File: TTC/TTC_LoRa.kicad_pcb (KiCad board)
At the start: 2 copper layers, 70 x 70 mm, 78 parts, among them J1 EPS 3V3, J2 MISSION, J3 SMA edge, J4 SWD TC2030, J5 OBC I2C, J6 OBC UART, J7 EPS 5V, J8 SPARE GPIO, J9 DIPOLE FEED, Q1 AO3401A, U1 TPS7A2033PDBVR, U2 RFM98W-433S2, U3 STM32F446RET6, U4 TMP102, Y1 8MHz, Y2 32.768kHz

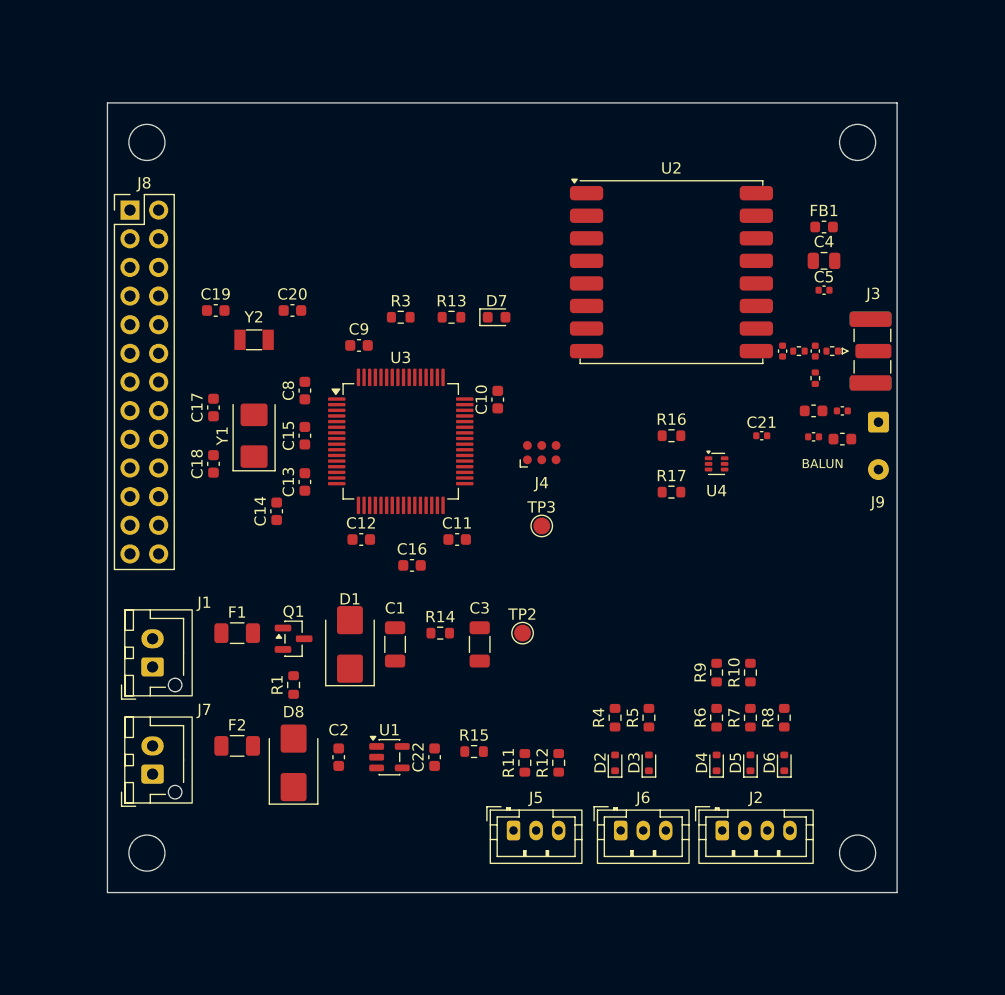
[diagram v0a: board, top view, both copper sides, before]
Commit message: TTC: fully routed LoRa board (checkpoint before review fixes)
Routed 2-layer layout of the TTC board: 1207 tracks, 297 vias, GND
poured on both layers. KiCad DRC: 0 violations, 0 unconnected,
schematic parity clean. README updated from "placed, not routed".

Co-Authored-By: Claude Opus 5.5 <noreply@anthropic.com>
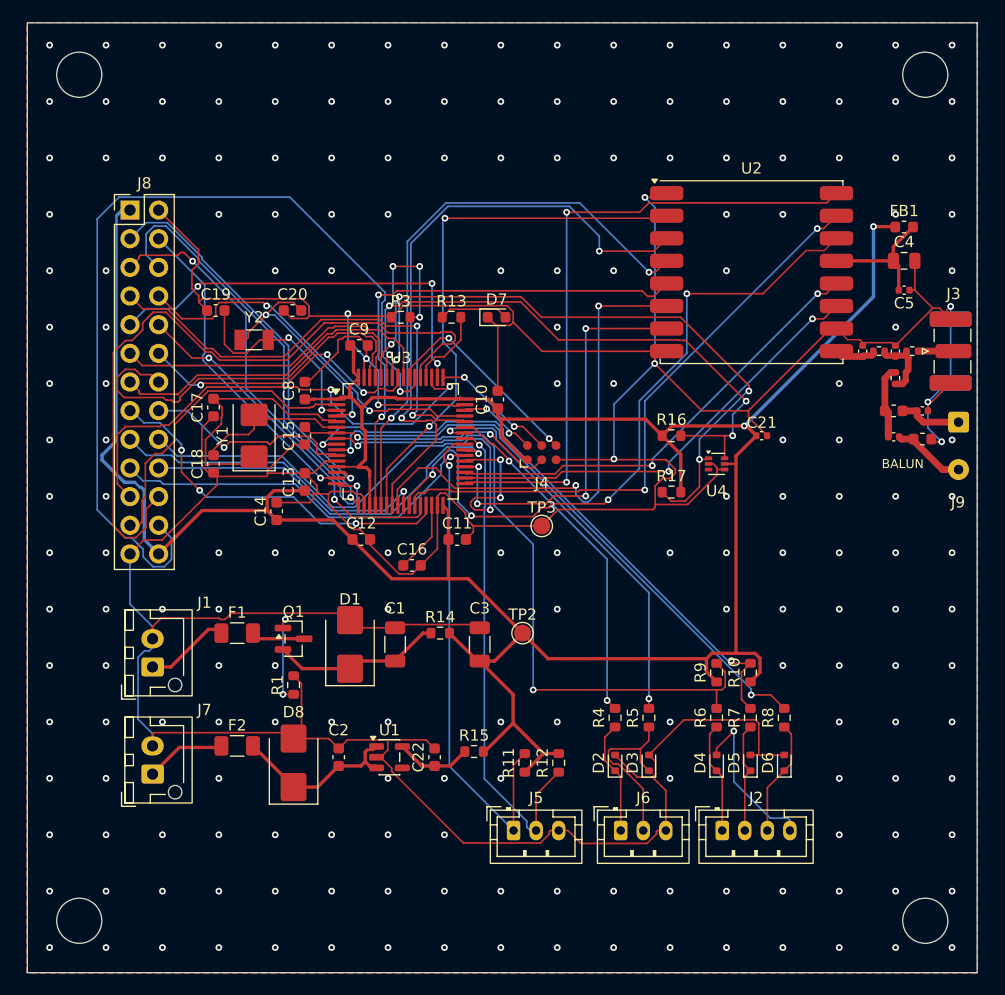
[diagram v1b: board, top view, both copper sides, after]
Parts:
- H1, H2, H3, H4: value M3 -> M4 stack; footprint MountingHole_3.2mm_M3 -> MountingHole_4mm
- moved H1 8.49 mm to (97.5, 97.5)
- moved H2 8.49 mm to (172.5, 97.5)
- moved H3 8.49 mm to (97.5, 172.5)
- moved H4 8.49 mm to (172.5, 172.5)
- moved C23 7.10 mm to (172.2, 127.3)
- moved C24 7.10 mm to (169.7, 129.6)
- moved C4 7.10 mm to (170.6, 114.0)
- moved C5 7.10 mm to (170.6, 116.6)
- moved C6 7.10 mm to (166.9, 122.0)
- moved C7 7.10 mm to (169.8, 122.0)
- moved FB1 7.10 mm to (170.6, 111.0)
- moved J3 7.10 mm to (175.0, 122.0)
- moved J9 7.10 mm to (175.4, 128.3)
- moved L1 7.10 mm to (169.7, 127.3)
- moved L2 7.10 mm to (172.2, 129.8)
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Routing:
- net GND: track 0.00 -> 457.0 mm, vias 0 -> 201
- net +3V3: track 0.00 -> 254.4 mm, vias 0 -> 2
- net /PD2: track 0.00 -> 80.2 mm, vias 0 -> 1
- net /PC12: track 0.00 -> 63.5 mm
- net /RFM_DIO0: track 0.00 -> 62.5 mm, vias 0 -> 4
- net /DEPLOY_SW: track 0.00 -> 59.2 mm, vias 0 -> 2
- net /RFM_DIO2: track 0.00 -> 57.6 mm, vias 0 -> 2
- net /I2C_SCL: track 0.00 -> 57.5 mm, vias 0 -> 4
- net /SPI1_MOSI: track 0.00 -> 54.9 mm, vias 0 -> 2
- net /RBF_IN: track 0.00 -> 54.2 mm, vias 0 -> 2
- net /RFM_DIO1: track 0.00 -> 53.3 mm, vias 0 -> 2
- net /BURN_EN: track 0.00 -> 52.8 mm, vias 0 -> 2
- net /I2C_SDA: track 0.00 -> 52.3 mm, vias 0 -> 4
- net /PC6: track 0.00 -> 51.9 mm, vias 0 -> 3
- net /SPI1_SCK: track 0.00 -> 51.7 mm, vias 0 -> 2
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- added copper zone on B.Cu, net GND
- added copper zone on F.Cu, net GND
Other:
- board size 70 x 70 mm -> 84.2 x 84.2 mm

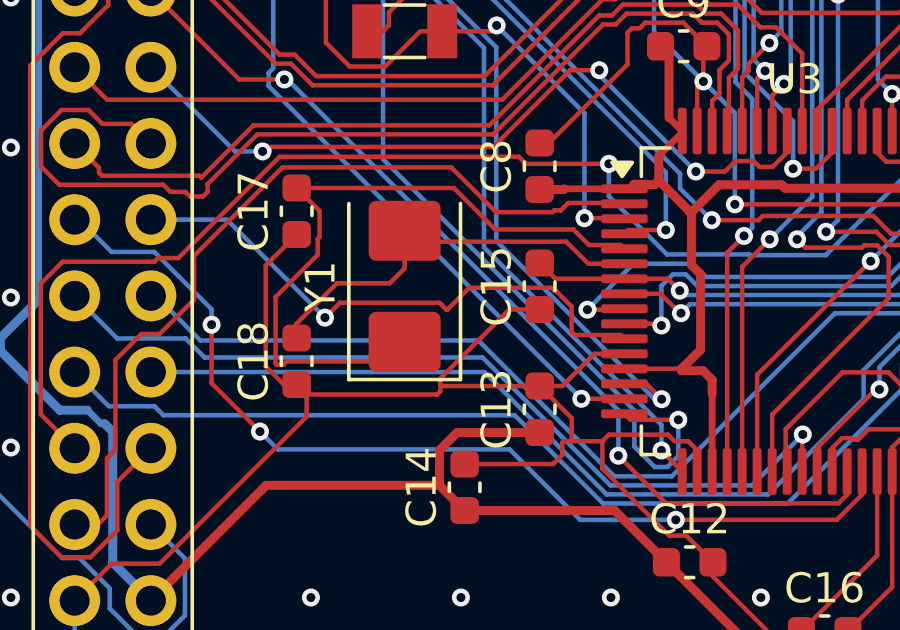
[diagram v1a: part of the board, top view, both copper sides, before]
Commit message: TTC: re-route 8 MHz crystal (Y1 rotated 180 deg)
Y1's pads were mirrored relative to the MCU pins, so PH0/PH1 crossed
and detoured. Rotating Y1 lines them up: PH0 23.2 -> 11.8 mm,
PH1 13.9 -> 16.7 mm (goes round the PC3 track), total 37.1 -> 28.5 mm,
no crossing. DRC: 0 violations, 0 unconnected.

Co-Authored-By: Claude Opus 5.5 <noreply@anthropic.com>
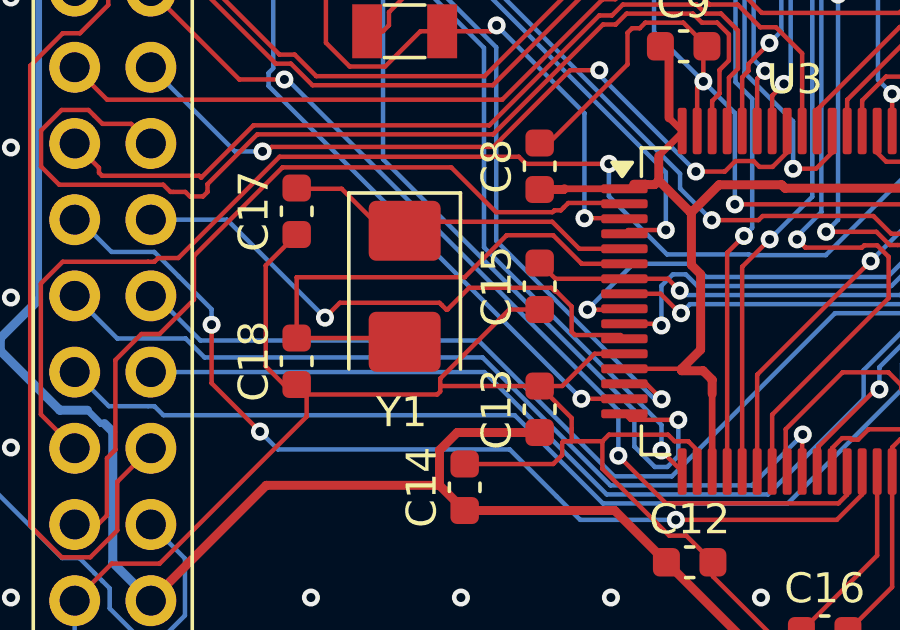
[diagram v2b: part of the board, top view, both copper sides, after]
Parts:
- turned Y1 to -90 degrees
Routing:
- net Net-(U3-PH0): track 23.2 -> 11.8 mm
- net Net-(U3-PH1): track 13.9 -> 16.7 mm
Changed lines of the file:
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@@
 	(footprint "Crystal:Crystal_SMD_5032-2Pin_5.0x3.2mm"
 		(layer "F.Cu")
-		(at 113 129.5 90)
+		(at 113 129.5 -90)
 		(descr "8 MHz HSE crystal (2-pad 5032); load caps from its CL")
 		(property "Reference" "Y1"
-			(at 0 -2.8 90)
+			(at 4.199999 0.1 0)
 			(layer "F.SilkS")
 			(effects
@@
 		)
 		(property "Value" "8MHz"
-			(at 0 2.8 90)
+			(at 0 2.8 270)
 			(layer "F.Fab")
 			(effects
@@
 		)
 		(property "Datasheet" ""
-			(at 0 0 90)
+			(at 0 0 270)
 			(layer "F.Fab")
 			(hide yes)
@@
 		)
 		(property "Description" "8 MHz HSE crystal (2-pad 5032); load caps from its CL"
-			(at 0 0 90)
+			(at 0 0 270)
 			(layer "F.Fab")
 			(hide yes)
@@
 		(duplicate_pad_numbers_are_jumpers no)
 		(fp_line
-			(start 2.76 -1.86)
-			(end -3.11 -1.86)
+			(start -3.11 1.86)
+			(end 2.76 1.86)
 			(stroke
 				(width 0.12)
@@
 		)
 		(fp_line
-			(start -3.11 1.86)
-			(end 2.76 1.86)
+			(start 2.76 -1.86)
+			(end -3.11 -1.86)
 			(stroke
 				(width 0.12)
@@
 		)
 		(fp_text user "${REFERENCE}"
-			(at 0 0 90)
+			(at 0 0 270)
 			(layer "F.Fab")
 			(effects
@@
 		)
 		(pad "1" smd roundrect
-			(at -1.85 0 90)
+			(at -1.85 0 270)
 			(size 2 2.4)
 			(layers "F.Cu" "F.Mask" "F.Paste")
@@
 		)
 		(pad "2" smd roundrect
-			(at 1.85 0 90)
+			(at 1.85 0 270)
 			(size 2 2.4)
 			(layers "F.Cu" "F.Mask" "F.Paste")
@@
 	)
 	(segment
-		(start 109.0579 132.0083)
-		(end 112.3417 132.0083)
-		(width 0.15)
-		(layer "F.Cu")
-		(net "Net-(U3-PH0)")
-	)
-	(segment
-		(start 110.1011 128.4511)
-		(end 108.6974 129.8548)
-		(width 0.15)
-		(layer "F.Cu")
-		(net "Net-(U3-PH0)")
-	)
-	(segment
-		(start 119.2406 128.1255)
-		(end 120.2005 128.1255)
-		(width 0.15)
-		(layer "F.Cu")
-		(net "Net-(U3-PH0)")
-	)
-	(segment
-		(start 109.4 126.225)
-		(end 114.6398 126.225)
-		(width 0.15)
-		(layer "F.Cu")
-		(net "Net-(U3-PH0)")
-	)
-	(segment
-		(start 112.3417 132.0083)
-		(end 113 131.35)
-		(width 0.15)
-		(layer "F.Cu")
-		(net "Net-(U3-PH0)")
-	)
-	(segment
-		(start 110.1633 127.8546)
-		(end 110.1011 127.9168)
-		(width 0.15)
-		(layer "F.Cu")
-		(net "Net-(U3-PH0)")
-	)
-	(segment
-		(start 109.4 126.225)
-		(end 110.1633 126.9883)
-		(width 0.15)
-		(layer "F.Cu")
-		(net "Net-(U3-PH0)")
-	)
-	(segment
-		(start 110.1011 127.9168)
-		(end 110.1011 128.4511)
+		(start 120.325 128.25)
+		(end 118.82 128.25)
 		(width 0.15)
 		(layer "F.Cu")
@@
 	)
 	(segment
-		(start 108.6974 129.8548)
-		(end 108.6974 132.0724)
+		(start 117.92 127.35)
+		(end 112 127.35)
 		(width 0.15)
 		(layer "F.Cu")
@@
 	)
 	(segment
-		(start 118.6233 127.6062)
-		(end 119.1426 128.1255)
+		(start 110.9 126.25)
+		(end 109.4 126.25)
 		(width 0.15)
 		(layer "F.Cu")
@@
 	)
 	(segment
-		(start 108.7395 132.1145)
-		(end 108.9517 132.1145)
+		(start 112 127.35)
+		(end 110.9 126.25)
 		(width 0.15)
 		(layer "F.Cu")
@@
 	)
 	(segment
-		(start 114.6398 126.225)
-		(end 116.021 127.6062)
+		(start 118.82 128.25)
+		(end 117.92 127.35)
 		(width 0.15)
 		(layer "F.Cu")
@@
 	)
 	(segment
-		(start 110.1633 126.9883)
-		(end 110.1633 127.8546)
-		(width 0.15)
-		(layer "F.Cu")
-		(net "Net-(U3-PH0)")
-	)
-	(segment
-		(start 108.9517 132.1145)
-		(end 109.0579 132.0083)
-		(width 0.15)
-		(layer "F.Cu")
-		(net "Net-(U3-PH0)")
-	)
-	(segment
-		(start 108.6974 132.0724)
-		(end 108.7395 132.1145)
-		(width 0.15)
-		(layer "F.Cu")
-		(net "Net-(U3-PH0)")
-	)
-	(segment
-		(start 119.1426 128.1255)
-		(end 119.2406 128.1255)
-		(width 0.15)
-		(layer "F.Cu")
-		(net "Net-(U3-PH0)")
-	)
-	(segment
-		(start 120.2005 128.1255)
-		(end 120.325 128.25)
-		(width 0.15)
-		(layer "F.Cu")
-		(net "Net-(U3-PH0)")
-	)
-	(segment
-		(start 116.021 127.6062)
-		(end 118.6233 127.6062)
-		(width 0.15)
-		(layer "F.Cu")
-		(net "Net-(U3-PH0)")
-	)
-	(segment
-		(start 112.5 129.4011)
-		(end 113 128.9011)
+		(start 116.4 127.8)
+		(end 115 129.199999)
 		(width 0.15)
 		(layer "F.Cu")
@@
 	)
 	(segment
-		(start 109.4 130.7442)
+		(start 109.4 129.199999)
 		(end 109.4 131.225)
 		(width 0.15)
@@
 	)
 	(segment
-		(start 111.4977 129.4011)
-		(end 110.7431 129.4011)
-		(width 0.15)
-		(layer "F.Cu")
-		(net "Net-(U3-PH1)")
-	)
-	(segment
-		(start 111.4977 129.4011)
-		(end 112.5 129.4011)
-		(width 0.15)
-		(layer "F.Cu")
-		(net "Net-(U3-PH1)")
-	)
-	(segment
-		(start 113 127.65)
-		(end 113 128.9011)
-		(width 0.15)
-		(layer "F.Cu")
-		(net "Net-(U3-PH1)")
-	)
-	(segment
-		(start 118.3864 128.0141)
-		(end 119.1223 128.75)
+		(start 115 129.199999)
+		(end 109.4 129.199999)
 		(width 0.15)
 		(layer "F.Cu")
@@
 	)
 	(segment
-		(start 110.7431 129.4011)
-		(end 109.4 130.7442)
+		(start 117.95 127.8)
+		(end 116.4 127.8)
 		(width 0.15)
 		(layer "F.Cu")
@@
 	)
 	(segment
-		(start 113.3641 128.0141)
-		(end 118.3864 128.0141)
+		(start 118.9 128.75)
+		(end 117.95 127.8)
 		(width 0.15)
 		(layer "F.Cu")
@@
 	)
 	(segment
-		(start 119.1223 128.75)
-		(end 120.325 128.75)
+		(start 120.325 128.75)
+		(end 118.9 128.75)
 		(width 0.15)
 		(layer "F.Cu")
@@
 	)
 	(segment
-		(start 113 127.65)
-		(end 113.3641 128.0141)
+		(start 109.4 131.225)
+		(end 112.2 131.225)
 		(width 0.15)
 		(layer "F.Cu")

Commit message: TTC: teardrops, RF via fence, courtyard check
- Teardrops on 470 pad/via joints for vibration robustness.
- 9 GND stitching vias along the antenna/balun tracks (297 -> 306 vias).
- DRC "missing courtyard" severity ignore -> warning (no footprint
  lacks a courtyard, none overlap).
- README: list of review changes.
DRC: 0 violations, 0 unconnected, schematic parity clean.

Co-Authored-By: Claude Opus 5.5 <noreply@anthropic.com>
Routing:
- net GND: vias 201 -> 210

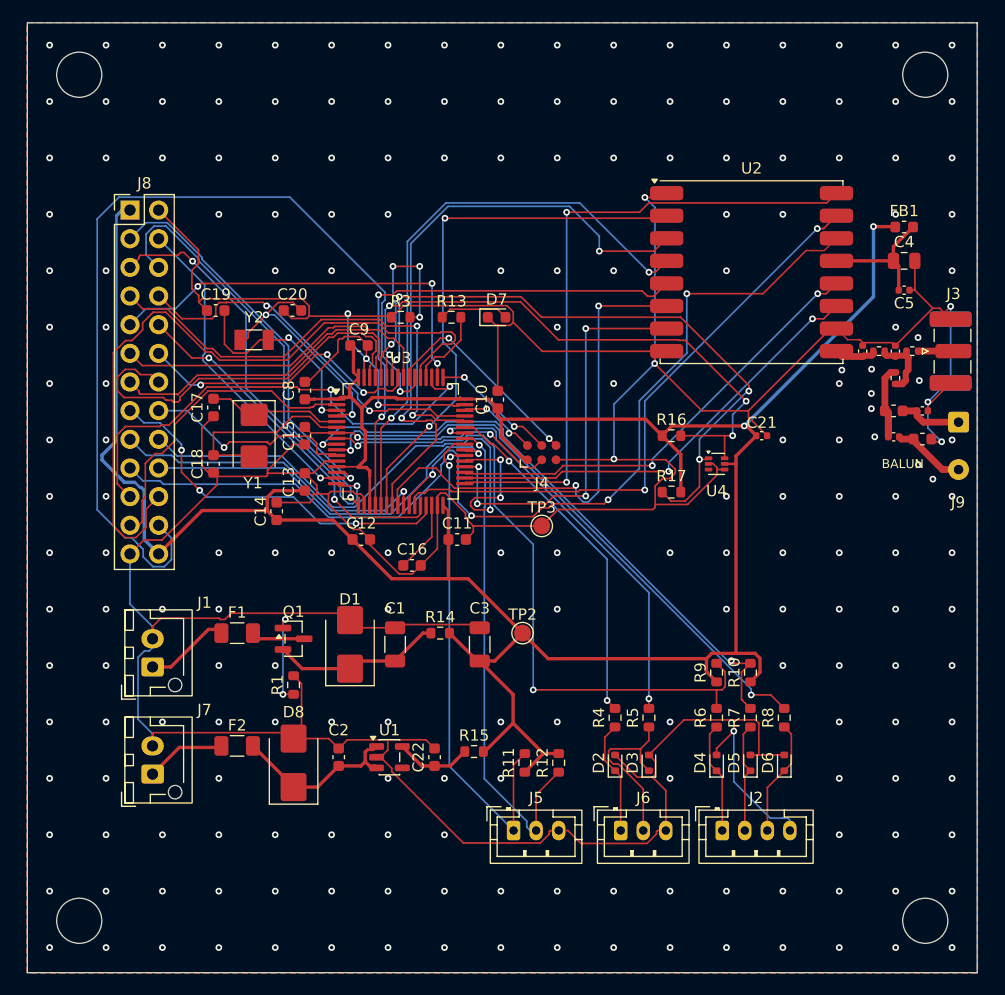
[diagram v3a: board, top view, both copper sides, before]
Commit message: TTC: make the spread auto layout the single TTC board
TTC/TTC_LoRa.kicad_pcb is now the spread, block-floorplanned layout
(previously TTC_auto/, commit b9867ab). TTC_auto/ removed so there is
one board in one place; every earlier layout stays in git history
(listed in TTC/README.md). README rewritten to describe this board.
DRC in the TTC project: 0 violations, 0 unconnected, parity clean.

Co-Authored-By: Claude Opus 5.5 <noreply@anthropic.com>
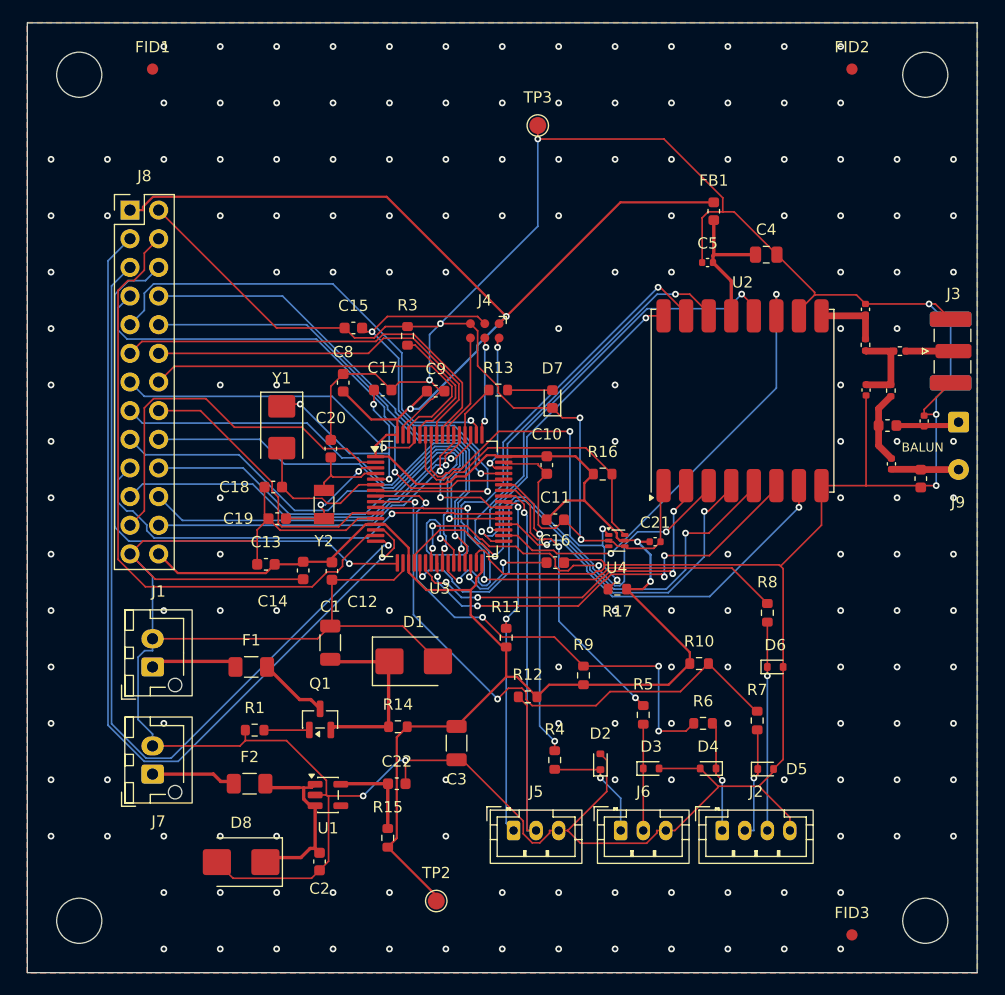
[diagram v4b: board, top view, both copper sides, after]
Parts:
- added FID1: Fiducial, Fiducial_1mm_Mask2mm, F.Cu at (104.0, 97.0)
- added FID2: Fiducial, Fiducial_1mm_Mask2mm, F.Cu at (166.0, 97.0)
- added FID3: Fiducial, Fiducial_1mm_Mask2mm, F.Cu at (166.0, 173.8)
- moved TP3 35.5 mm to (138.2, 102.0), turned to -90 degrees
- moved TP2 25.0 mm to (129.2, 170.8), turned to 180 degrees
- moved C19 19.2 mm to (115.0, 136.8)
- moved C5 17.6 mm to (153.2, 114.2), turned to 180 degrees
- moved FB1 16.9 mm to (153.8, 109.6), turned to -90 degrees
- moved Y2 15.9 mm to (119.2, 135.6), turned to -90 degrees
- moved C17 15.1 mm to (124.4, 125.5), turned to 180 degrees
- moved C21 13.3 mm to (148.6, 138.9)
- moved C20 12.7 mm to (119.8, 130.7), turned to -90 degrees
- moved C16 12.7 mm to (139.7, 140.8)
- moved C4 12.2 mm to (158.4, 113.5)
- moved J4 11.9 mm to (133.4, 120.2), turned to 180 degrees
- moved R9 11.8 mm to (142.2, 150.8)
- moved U2 11.4 mm to (156.3, 126.4), turned to 90 degrees
- moved R11 11.2 mm to (135.3, 147.4)
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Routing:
- net /PD2: track 80.2 -> 30.6 mm
- net /PA0: track 34.9 -> 81.2 mm
- net GND: track 457.0 -> 499.8 mm, vias 210 -> 172
- net /PA2: track 37.7 -> 76.0 mm, vias 2 -> 1
- net /PC12: track 63.5 -> 31.7 mm, vias 0 -> 1
- net /RFM_DIO2: track 57.6 -> 30.0 mm
- net /PA1: track 28.7 -> 56.3 mm, vias 1 -> 0
- net /I2C_SDA: track 52.3 -> 27.9 mm, vias 4 -> 0
- net /I2C_SCL: track 57.5 -> 36.8 mm, vias 4 -> 3
- net +3V3: track 254.4 -> 234.7 mm, vias 2 -> 4
- net /NRST: track 23.3 -> 42.3 mm
- net /SPI1_MOSI: track 54.9 -> 36.7 mm, vias 2 -> 4
- net /RFM_DIO0: track 62.5 -> 44.4 mm, vias 4 -> 2
- net /PC5: track 28.8 -> 44.7 mm
- net /SPI1_MISO: track 48.3 -> 33.2 mm, vias 2 -> 4
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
